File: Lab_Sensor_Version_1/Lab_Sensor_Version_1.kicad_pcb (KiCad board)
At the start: 2 copper layers, 94.2 x 66 mm, 28 parts, among them U1 ESP32-POE, U2 AM2302, U3 SSD1306, U4 INMP441

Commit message: Updated Cad Models & Board Layout
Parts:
- added H1: MountingHole, MountingHole:MountingHole_2.2mm_M2, F.Cu at (107.0, 109.2)
- added H2: MountingHole, MountingHole:MountingHole_2.2mm_M2, F.Cu at (147.5, 109.2)
- added H3: MountingHole, MountingHole:MountingHole_2.2mm_M2, F.Cu at (165.8, 50.2)
- U1: value ESP32-POE -> MODULE_ESP32-POE
- moved U1 0.89 mm to (115.4, 61.8)
- moved TP1 0.75 mm to (77.0, 77.8)
- moved TP2 0.50 mm to (77.0, 81.0)
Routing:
- net GND: track 182.7 -> 0.00 mm, vias 0 -> 3
- net Net-(U1-GPIO0): track 45.4 -> 40.6 mm
- net Net-(U1-GPI35): track 16.6 -> 15.3 mm
- net Net-(U1-GPIO1): track 44.0 -> 42.8 mm
- net Net-(U1-GPIO15): track 15.6 -> 14.5 mm
- net Net-(U1-GPIO33): track 16.4 -> 15.5 mm
- net Net-(U1-GPIO13): track 34.5 -> 33.6 mm
- net Net-(U1-GPIO32): track 25.9 -> 25.0 mm
- net Net-(U1-GPIO16): track 35.5 -> 34.6 mm
- net Net-(U1-GPIO14): track 25.0 -> 24.1 mm
- net Net-(U1-GPIO3): track 37.3 -> 36.4 mm
- net Net-(U1-GPIO2): track 37.3 -> 36.5 mm
- net +3.3V: track 135.0 -> 135.9 mm, vias 2 -> 0
- added copper zone on B.Cu, net GND
- added copper zone on F.Cu, net GND
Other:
- board text added: "Noise"
- board text added: "Status"
- board text added: "Temp"

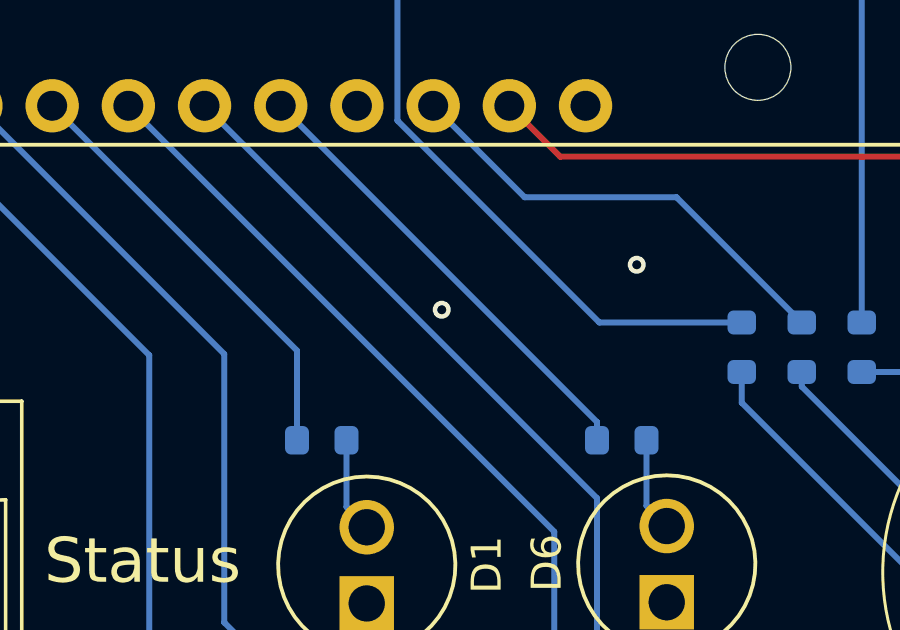
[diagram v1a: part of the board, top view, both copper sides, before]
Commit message: Added CAD models for render
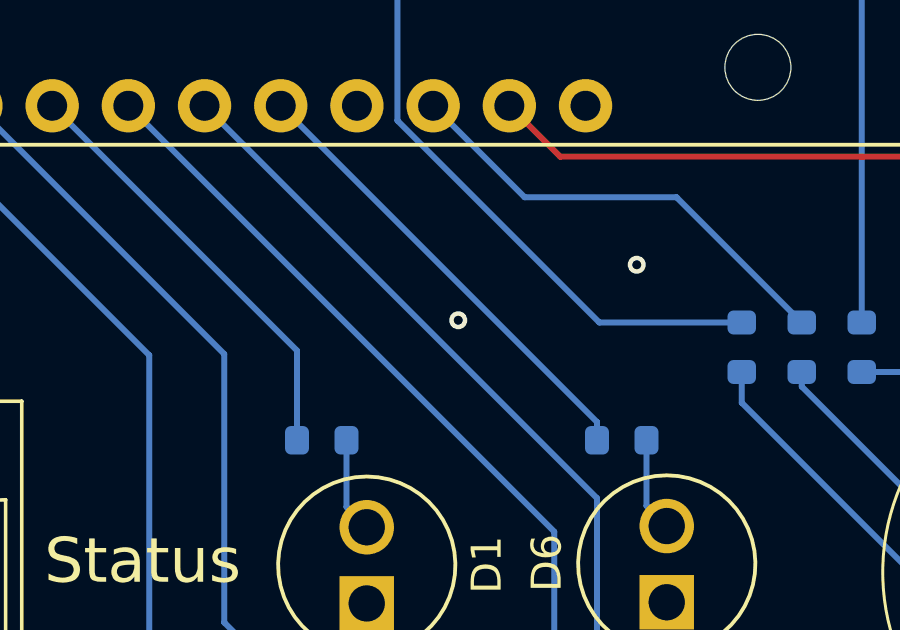
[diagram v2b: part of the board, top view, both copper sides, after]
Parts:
- TP1, TP2: value 5002 -> KEYSTONE_5002
- U1: value MODULE_ESP32-POE -> ESP32-POE
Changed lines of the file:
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@@
 			)
 		)
-		(property "Value" "5002"
+		(property "Value" "KEYSTONE_5002"
 			(at 3.2832 2.2064 90)
 			(layer "F.Fab")
@@
 		)
 		(embedded_fonts no)
+		(model "C:/Users/sidko/Desktop/GitHub/PCB-Projects/KiCad/Misc/5002.step"
+			(offset
+				(xyz 0 0 0)
+			)
+			(scale
+				(xyz 1 1 1)
+			)
+			(rotate
+				(xyz -90 -0 -0)
+			)
+		)
 	)
 	(footprint "Custom_Parts:Standard_LED_Throughhole"
@@
 		)
 		(embedded_fonts no)
+		(model "C:/Users/sidko/Desktop/GitHub/PCB-Projects/KiCad/Misc/LED.STEP"
+			(offset
+				(xyz 0 0 0)
+			)
+			(scale
+				(xyz 1 1 1)
+			)
+			(rotate
+				(xyz -90 -0 -0)
+			)
+		)
 	)
 	(footprint "Custom_Parts:INMP441"
@@
 		)
 		(embedded_fonts no)
-		(model "C:/Users/sidko/Downloads/INMP441 I2S Microphone Module v15.step"
+		(model "C:/Users/sidko/Desktop/GitHub/PCB-Projects/KiCad/Misc/INMP441.step"
 			(offset
 				(xyz 0 0 1)
@@
 			)
 		)
-		(property "Value" "5002"
+		(property "Value" "KEYSTONE_5002"
 			(at 3.2832 2.2064 90)
 			(layer "F.Fab")
@@
 		)
 		(embedded_fonts no)
+		(model "C:/Users/sidko/Desktop/GitHub/PCB-Projects/KiCad/Misc/5002.step"
+			(offset
+				(xyz 0 0 0)
+			)
+			(scale
+				(xyz 1 1 1)
+			)
+			(rotate
+				(xyz -90 -0 -0)
+			)
+		)
 	)
 	(footprint "Custom_Parts:ESP32-POE"
@@
 			)
 		)
-		(property "Value" "MODULE_ESP32-POE"
+		(property "Value" "ESP32-POE"
 			(at -3.84 41.115 90)
 			(layer "F.Fab")
@@
 		)
 		(embedded_fonts no)
+		(model "C:/Users/sidko/Desktop/GitHub/PCB-Projects/KiCad/Misc/LED.STEP"
+			(offset
+				(xyz 0 0 0)
+			)
+			(scale
+				(xyz 1 1 1)
+			)
+			(rotate
+				(xyz -90 -0 -0)
+			)
+		)
 	)
 	(footprint "Custom_Parts:Standard_LED_Throughhole"
@@
 		)
 		(embedded_fonts no)
+		(model "C:/Users/sidko/Desktop/GitHub/PCB-Projects/KiCad/Misc/LED.STEP"
+			(offset
+				(xyz 0 0 0)
+			)
+			(scale
+				(xyz 1 1 1)
+			)
+			(rotate
+				(xyz -90 -0 -0)
+			)
+		)
 	)
 	(footprint "Sensor:ASAIR_AM2302_P2.54mm_Lead2.75mm_TabDown"
@@
 		)
 		(embedded_fonts no)
-		(model "${KICAD9_3DMODEL_DIR}/Sensor.3dshapes/ASAIR_AM2302_P2.54mm_Lead2.75mm_TabDown.step"
+		(model "C:/Users/sidko/Desktop/GitHub/PCB-Projects/KiCad/Misc/DHT22.stp"
 			(offset
-				(xyz 0 0 0)
+				(xyz 22.75 3.75 0)
 			)
 			(scale
@@
 			)
 			(rotate
-				(xyz 0 0 0)
+				(xyz -0 -0 90)
 			)
 		)
@@
 		)
 		(embedded_fonts no)
+		(model "C:/Users/sidko/Desktop/GitHub/PCB-Projects/KiCad/Misc/SSD1306.step"
+			(offset
+				(xyz 34.5 3.4 3.5)
+			)
+			(scale
+				(xyz 1 1 1)
+			)
+			(rotate
+				(xyz -0 -0 -0)
+			)
+		)
 	)
 	(footprint "Custom_Parts:Standard_LED_Throughhole"
@@
 		)
 		(embedded_fonts no)
+		(model "C:/Users/sidko/Desktop/GitHub/PCB-Projects/KiCad/Misc/LED.STEP"
+			(offset
+				(xyz 0 0 0)
+			)
+			(scale
+				(xyz 1 1 1)
+			)
+			(rotate
+				(xyz -90 -0 -0)
+			)
+		)
 	)
 	(footprint "Custom_Parts:Standard_LED_Throughhole"
@@
 		)
 		(embedded_fonts no)
+		(model "C:/Users/sidko/Desktop/GitHub/PCB-Projects/KiCad/Misc/LED.STEP"
+			(offset
+				(xyz 0 0 0)
+			)
+			(scale
+				(xyz 1 1 1)
+			)
+			(rotate
+				(xyz -90 -0 -0)
+			)
+		)
 	)
 	(footprint "Resistor_SMD:R_0603_1608Metric"
@@
 		)
 		(embedded_fonts no)
+		(model "C:/Users/sidko/Desktop/GitHub/PCB-Projects/KiCad/Misc/LED.STEP"
+			(offset
+				(xyz 0 0 0)
+			)
+			(scale
+				(xyz 1 1 1)
+			)
+			(rotate
+				(xyz -90 -0 -0)
+			)
+		)
 	)
 	(footprint "Capacitor_SMD:C_0603_1608Metric"
@@
 	)
 	(via
-		(at 117.5 81.25)
+		(at 118.05 81.6)
 		(size 0.6)
 		(drill 0.3)

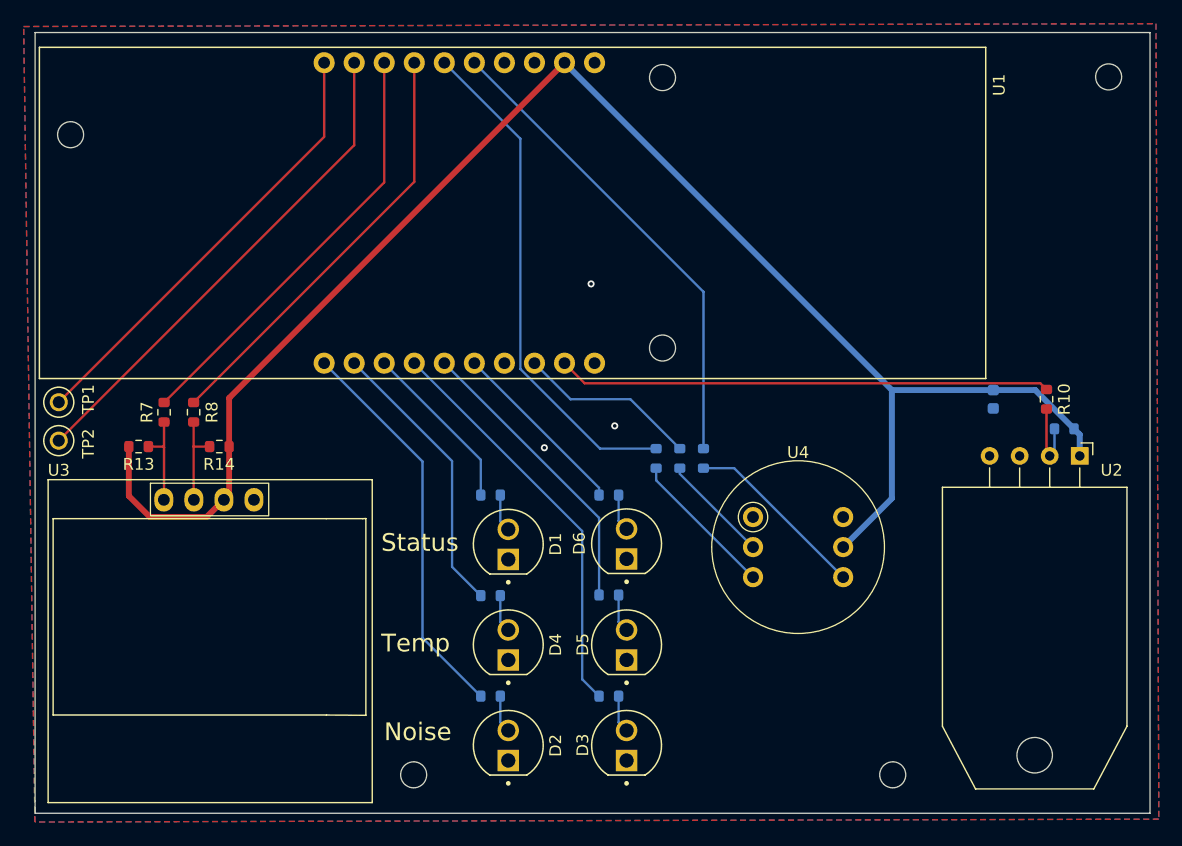
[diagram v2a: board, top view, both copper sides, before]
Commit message: improved trace sizes
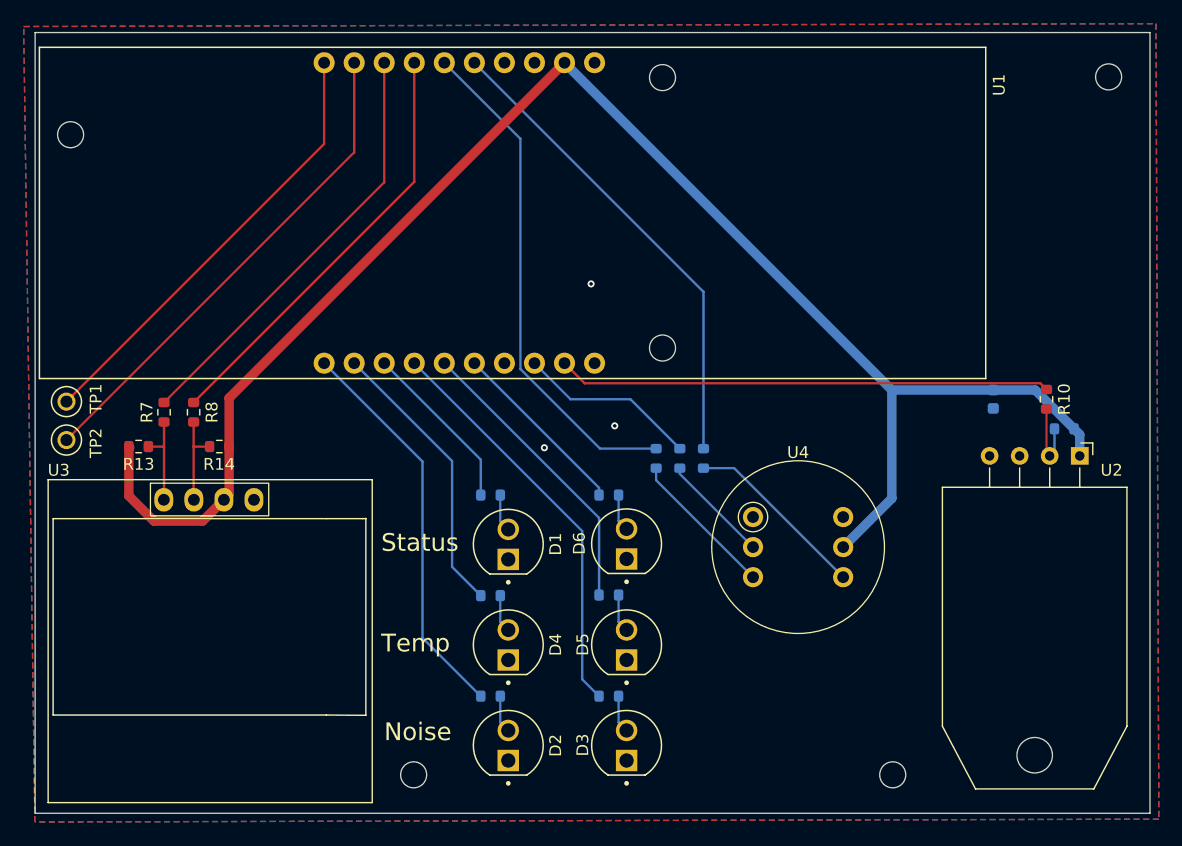
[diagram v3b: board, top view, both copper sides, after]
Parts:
- moved TP1 0.65 mm to (77.7, 77.7)
- moved TP2 0.65 mm to (77.7, 81.0)
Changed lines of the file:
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@@
 	(footprint "Custom_Parts:5002"
 		(layer "F.Cu")
-		(at 77 81 -90)
+		(at 77.65 80.95 -90)
 		(property "Reference" "TP2"
 			(at 0.25 -2.5 90)
@@
 	(footprint "Custom_Parts:5002"
 		(layer "F.Cu")
-		(at 77 77.75 -90)
+		(at 77.65 77.7 -90)
 		(property "Reference" "TP1"
 			(at -0.25 -2.5 90)
@@
 	)
 	(segment
-		(start 119.753 49.05)
-		(end 91.4 77.403)
-		(width 0.5)
+		(start 85.05 87.8)
+		(end 82.925 85.675)
+		(width 0.8)
 		(layer "F.Cu")
 		(net 1)
 	)
 	(segment
-		(start 82.925 85.675)
-		(end 82.925 81.5)
-		(width 0.5)
+		(start 119.753 49.05)
+		(end 91.4 77.403)
+		(width 0.8)
 		(layer "F.Cu")
 		(net 1)
@@
 		(start 83 81.575)
 		(end 82.925 81.5)
-		(width 0.5)
+		(width 0.8)
 		(layer "F.Cu")
 		(net 1)
@@
 		(start 91.4 81.5)
 		(end 91.4 85.56)
-		(width 0.5)
+		(width 0.8)
 		(layer "F.Cu")
 		(net 1)
 	)
 	(segment
-		(start 91.4 85.56)
-		(end 90.96 86)
-		(width 0.5)
+		(start 90.96 86)
+		(end 89.16 87.8)
+		(width 0.8)
 		(layer "F.Cu")
 		(net 1)
 	)
 	(segment
-		(start 91.4 77.403)
-		(end 91.4 81.5)
-		(width 0.5)
+		(start 91.4 85.56)
+		(end 90.96 86)
+		(width 0.8)
 		(layer "F.Cu")
 		(net 1)
 	)
 	(segment
-		(start 90.96 86)
-		(end 89.509 87.451)
-		(width 0.5)
+		(start 82.925 85.675)
+		(end 82.925 81.5)
+		(width 0.8)
 		(layer "F.Cu")
 		(net 1)
 	)
 	(segment
-		(start 89.509 87.451)
-		(end 84.701 87.451)
-		(width 0.5)
+		(start 91.4 77.403)
+		(end 91.4 81.5)
+		(width 0.8)
 		(layer "F.Cu")
 		(net 1)
 	)
 	(segment
-		(start 84.701 87.451)
-		(end 82.925 85.675)
-		(width 0.5)
+		(start 89.16 87.8)
+		(end 85.05 87.8)
+		(width 0.8)
 		(layer "F.Cu")
 		(net 1)
@@
 		(start 147.428 85.882)
 		(end 143.31 90)
-		(width 0.5)
+		(width 0.8)
 		(layer "B.Cu")
 		(net 1)
@@
 		(start 163.31 82.2925)
 		(end 163.31 80.485)
-		(width 0.5)
+		(width 0.8)
 		(layer "B.Cu")
 		(net 1)
@@
 		(start 147.428 76.725)
 		(end 156 76.725)
-		(width 0.5)
+		(width 0.8)
 		(layer "B.Cu")
 		(net 1)
@@
 		(start 163.31 80.485)
 		(end 162.825 80)
-		(width 0.5)
+		(width 0.8)
 		(layer "B.Cu")
 		(net 1)
@@
 		(start 156 76.725)
 		(end 159.55 76.725)
-		(width 0.5)
+		(width 0.8)
 		(layer "B.Cu")
 		(net 1)
@@
 		(start 159.55 76.725)
 		(end 162.825 80)
-		(width 0.5)
+		(width 0.8)
 		(layer "B.Cu")
 		(net 1)
@@
 		(start 119.753 49.05)
 		(end 147.428 76.725)
-		(width 0.5)
+		(width 0.8)
 		(layer "B.Cu")
 		(net 1)
@@
 		(start 147.428 76.725)
 		(end 147.428 85.882)
-		(width 0.5)
+		(width 0.8)
 		(layer "B.Cu")
 		(net 1)
@@
 	)
 	(segment
-		(start 101.973 56.027)
-		(end 77 81)
+		(start 101.973 49.05)
+		(end 101.973 56.627)
 		(width 0.2)
 		(layer "F.Cu")
@@
 	)
 	(segment
-		(start 101.973 49.05)
-		(end 101.973 56.027)
+		(start 101.973 56.627)
+		(end 77.65 80.95)
 		(width 0.2)
 		(layer "F.Cu")
@@
 	)
 	(segment
-		(start 99.433 55.317)
-		(end 77 77.75)
+		(start 99.433 49.05)
+		(end 99.433 55.917)
 		(width 0.2)
 		(layer "F.Cu")
@@
 	)
 	(segment
-		(start 99.433 49.05)
-		(end 99.433 55.317)
+		(start 99.433 55.917)
+		(end 77.65 77.7)
 		(width 0.2)
 		(layer "F.Cu")

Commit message: Changed pinout to work with Code
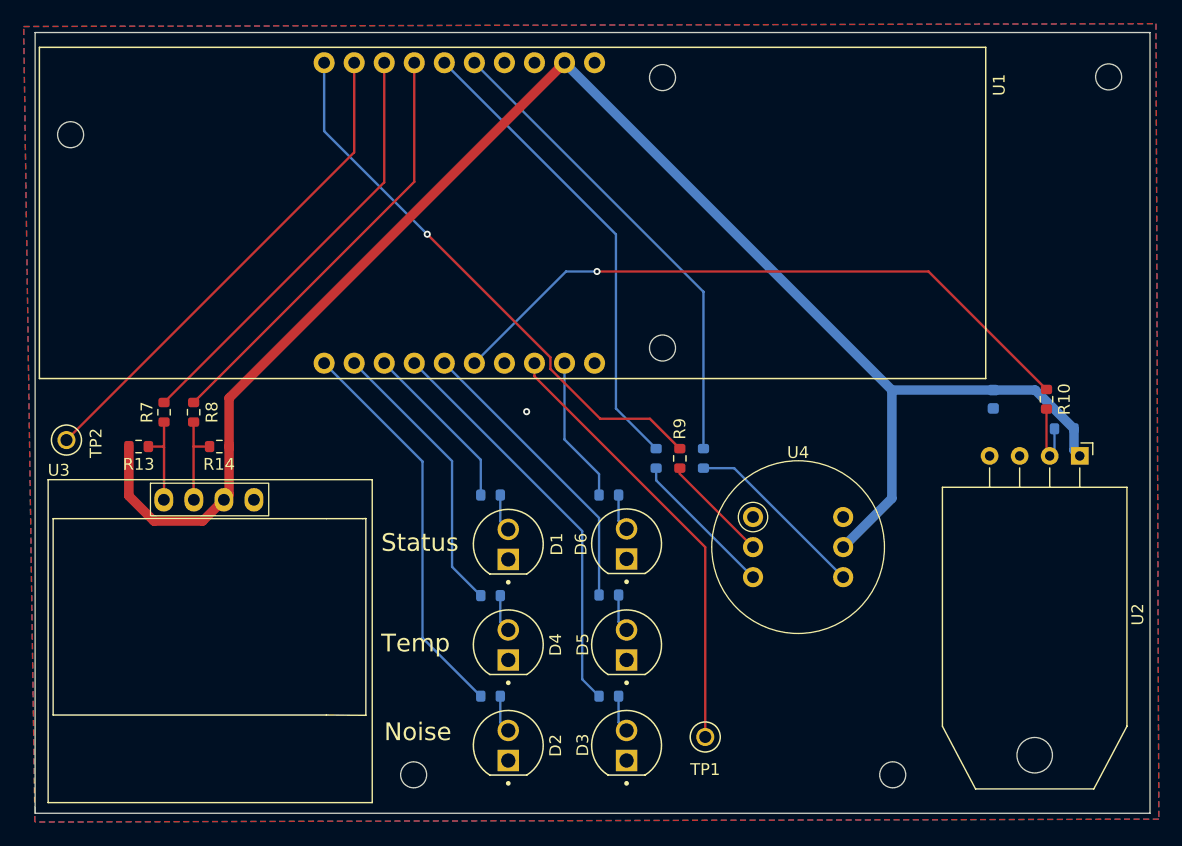
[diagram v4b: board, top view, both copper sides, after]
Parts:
- R9: moved to F.Cu
- TP1, TP2: value KEYSTONE_5002 -> 5002
- moved TP1 61.0 mm to (131.7, 106.0), turned to 180 degrees
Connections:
- R10 pad 1: Net-(U1-GPI36) -> Net-(U1-GPIO33)
- R12 pad 1: Net-(U1-GPIO33) -> Net-(U1-GPI36)
- R9 pad 1: Net-(U1-GPI35) -> Net-(U1-GPIO5)
- TP1 pad TP: Net-(U1-GPIO5) -> Net-(U1-GPI35)
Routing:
- net Net-(U1-GPIO33): track 15.5 -> 55.7 mm, vias 0 -> 1
- net Net-(U1-GPI36): track 41.7 -> 12.4 mm
- net Net-(U1-GPI35): track 15.3 -> 37.6 mm
- net Net-(U1-GPIO5): track 37.7 -> 47.5 mm, vias 0 -> 1
- net Net-(U1-GPIO1): track 42.8 -> 40.0 mm
- net GND: vias 3 -> 1
